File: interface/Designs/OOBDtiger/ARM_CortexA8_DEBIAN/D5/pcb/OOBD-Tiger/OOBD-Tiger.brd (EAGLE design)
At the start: 63.4 x 38.2 mm, 88 parts, among them IC3 DS1307, IC4 DS3231, Q2 32.768kHz, U1 SY6280, U10 MP1482DS, U2 SN65HVD230(SO8), U6 SN65HVD230(SO8)

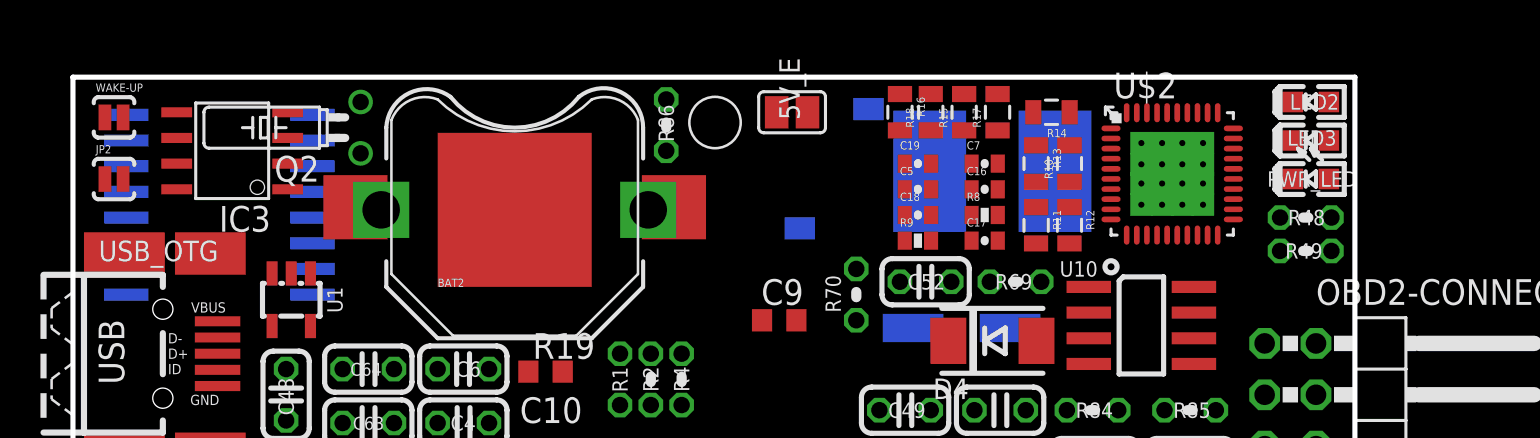
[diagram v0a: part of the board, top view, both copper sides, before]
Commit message: - delete further unneeded files(.lbr) - fix and rename Olimex_Connector.lbr to OOBDtiger-Connector.lbr - fix inconsistency error between schematic and pcb - create regular Projects for AM3352-SOM-EVB and OOBD-Tiger.brd - fix all ERC errors (only some uncritical warnings are open) - update OOBD-Tiger.pdf to visualize current status - fix TLV320AIC3107.lbr (=> but sym and dev is missing)
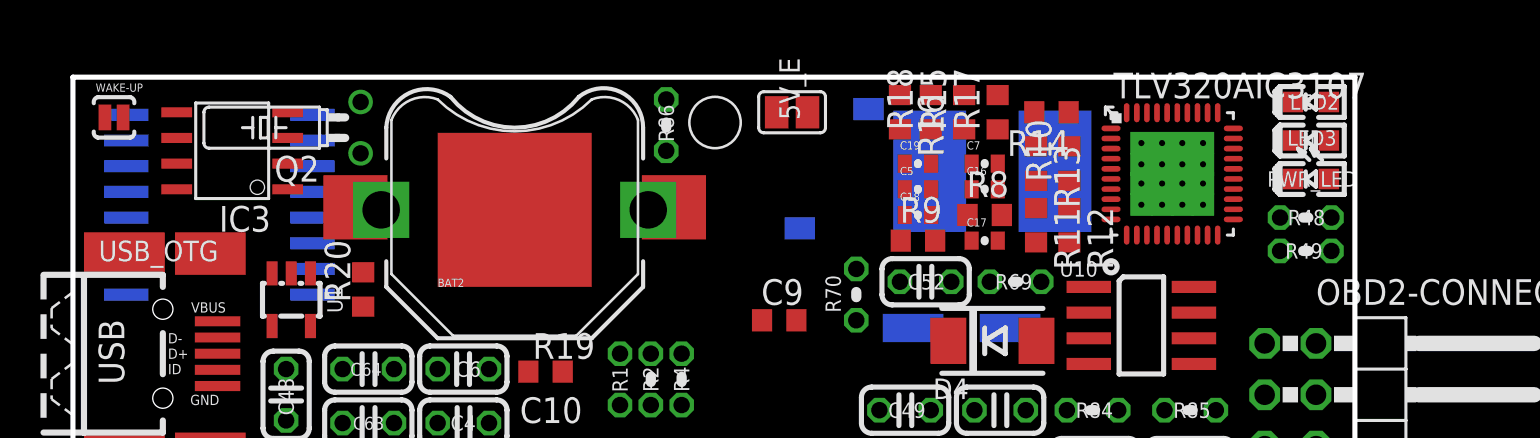
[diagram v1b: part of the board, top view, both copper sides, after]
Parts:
- removed JP2: (no value), SparkFun:SJ_2S-NO
- added R20: 10k, rcl:R0603
- AM3352-SOM-EVB-PLATFORM: device Tiger-connector_new:AM3352-SOM-EVB -> OOBDtiger-Connector:OOBD-TIGER-AM3352-SOM
- R10, R11, R12, R13, R14, R15, R16, R17, R18: device SparkFun-Passives:0805 -> resistor:R0603
- R8, R9: device SparkFun-Passives:0402-RES -> resistor:R0603
- renumbered U$2 to TLV320AIC3107
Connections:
- net P0_12/I2C2_SDA renamed DCAN0_TX
- net P0_13/I2C2_SCL renamed DCAN0_RX
- net P1_8/UART4_RXD renamed DCAN1_TX
- net P1_9/UART4_TXD renamed DCAN1_RX
- net USB1-VBUS renamed USB1_VBUS
- net USB1-VBUS1 renamed USB1_VBUS1
- removed net 3.3V: C16.1, C17.1, R8.2, R9.2, TLV320AIC3107.13, TLV320AIC3107.18, TLV320AIC3107.40
- removed net AIN4: AM3352-SOM-EVB-PLATFORM.4-35
- removed net AIN5: AM3352-SOM-EVB-PLATFORM.4-37
- removed net AIN6: AM3352-SOM-EVB-PLATFORM.4-38
- removed net AIN7: AM3352-SOM-EVB-PLATFORM.4-36
- removed net GNDA: AM3352-SOM-EVB-PLATFORM.4-40
- removed net JTAG_TCK: AM3352-SOM-EVB-PLATFORM.4-29
- removed net JTAG_TDI: AM3352-SOM-EVB-PLATFORM.4-31
- removed net JTAG_TDO: AM3352-SOM-EVB-PLATFORM.4-33
- removed net JTAG_TMS: AM3352-SOM-EVB-PLATFORM.4-32
- removed net JTAG_TRST: AM3352-SOM-EVB-PLATFORM.4-30
- removed net MMC0-SDCD#/EMU4: AM3352-SOM-EVB-PLATFORM.3-17
- removed net N$13: MS-CAN.2
- removed net N$30: L6.2
- removed net NNMI: AM3352-SOM-EVB-PLATFORM.3-22
- removed net OUT: JP2.2
- removed net P0_0/EMDIO: AM3352-SOM-EVB-PLATFORM.3-38
- removed net P0_1/EMDC: AM3352-SOM-EVB-PLATFORM.3-36
- removed net P0_14/UART1_RXD: AM3352-SOM-EVB-PLATFORM.4-6
- removed net P0_15/UART1_TXD: AM3352-SOM-EVB-PLATFORM.4-5
- removed net P0_16/ETXD3: AM3352-SOM-EVB-PLATFORM.3-29
- removed net P0_17/ETXD2: AM3352-SOM-EVB-PLATFORM.3-27
- removed net P0_2/SPI0_SCLK: AM3352-SOM-EVB-PLATFORM.4-11
- removed net P0_20/EMU3: AM3352-SOM-EVB-PLATFORM.4-22
- removed net P0_21/ETXD1: AM3352-SOM-EVB-PLATFORM.3-25
- removed net P0_28/ETXD0: AM3352-SOM-EVB-PLATFORM.3-23
- removed net P0_29/EPHY-RST#/RFCLK: AM3352-SOM-EVB-PLATFORM.3-40
- removed net P0_3/SPI0_D0(MISO): AM3352-SOM-EVB-PLATFORM.4-9
- removed net P0_4/SPI0_D1(MOSI): AM3352-SOM-EVB-PLATFORM.4-10
- removed net P0_5/SPI0_CS0: AM3352-SOM-EVB-PLATFORM.4-12
- removed net P0_7/PWM0_OUT: AM3352-SOM-EVB-PLATFORM.4-27
- removed net P2_18/ERXD3: AM3352-SOM-EVB-PLATFORM.3-30
- removed net P2_19/ERXD2: AM3352-SOM-EVB-PLATFORM.3-28
- removed net P2_20/ERXD1: AM3352-SOM-EVB-PLATFORM.3-26
- removed net P2_21/ERXD0: AM3352-SOM-EVB-PLATFORM.3-24
- removed net P3_0/ECOL: AM3352-SOM-EVB-PLATFORM.3-37
- removed net P3_1/ECRS: AM3352-SOM-EVB-PLATFORM.3-39
- removed net P3_10/ERXCK: AM3352-SOM-EVB-PLATFORM.3-34
- removed net P3_14/SPI1_CLK: AM3352-SOM-EVB-PLATFORM.4-19
- removed net P3_15/SPI1_D0(MISO): AM3352-SOM-EVB-PLATFORM.4-17
- removed net P3_16/SPI1_D1(MOSI): AM3352-SOM-EVB-PLATFORM.4-18
- removed net P3_17/SPI1_CS0: AM3352-SOM-EVB-PLATFORM.4-20
- removed net P3_18/LED1: AM3352-SOM-EVB-PLATFORM.4-21
- removed net P3_2/ERXERR: AM3352-SOM-EVB-PLATFORM.3-35
- removed net P3_3/ETXEN: AM3352-SOM-EVB-PLATFORM.3-31
- removed net P3_4/ERXDV: AM3352-SOM-EVB-PLATFORM.3-32
- removed net P3_5/I2C0-SDA: AM3352-SOM-EVB-PLATFORM.4-16
- removed net P3_6/I2C0-SCL: AM3352-SOM-EVB-PLATFORM.4-15
- removed net P3_7/EMU0: AM3352-SOM-EVB-PLATFORM.4-25
- removed net P3_8/EMU1: AM3352-SOM-EVB-PLATFORM.4-26, R40.2, R7.2
- removed net P3_9/ETXCK: AM3352-SOM-EVB-PLATFORM.3-33
- removed net SCL: IC3.6, IC4.16, R8.1, TLV320AIC3107.1
- removed net SDA: IC3.5, IC4.15
- removed net V+: C9.2, IC4.2, R19.2
- removed net VDDA_ADC: AM3352-SOM-EVB-PLATFORM.4-39
- removed net VREFP: AM3352-SOM-EVB-PLATFORM.4-34
- new net +3V3: C16.1, C17.1, C9.2, IC4.2, R20.2, R8.2, R9.2, TLV320AIC3107.13, TLV320AIC3107.18, TLV320AIC3107.40
- new net HS-CAN_RS: AM3352-SOM-EVB-PLATFORM.4-26, R7.2
- new net I2C0-SCL: AM3352-SOM-EVB-PLATFORM.4-15, IC3.6, IC4.16, R8.1, TLV320AIC3107.1
- new net I2C0-SDA: AM3352-SOM-EVB-PLATFORM.4-16, IC3.5, IC4.15, R9.1, TLV320AIC3107.2
- new net MS-CAN_RS: AM3352-SOM-EVB-PLATFORM.4-25, R40.2
- net +5V: now also R19.2
- net AUD_BCLK: now also AM3352-SOM-EVB-PLATFORM.4-19
- net AUD_DIN: now also AM3352-SOM-EVB-PLATFORM.4-18
- net AUD_DOUT: now also AM3352-SOM-EVB-PLATFORM.4-20
- net AUD_MCLK: now also AM3352-SOM-EVB-PLATFORM.4-24
- net AUD_WCLK: now also AM3352-SOM-EVB-PLATFORM.4-17
- net GND: now also AM3352-SOM-EVB-PLATFORM.4-40
- net N$10: now also MS-CAN.2, R42.1; no longer R9.1, TLV320AIC3107.2
- net N$27: now also IC4.3, R20.1; no longer IC4.4
- net N$29: now also L6.2
- net N$3: no longer IC4.3, JP2.1
- net P3_20/LED2: no longer AM3352-SOM-EVB-PLATFORM.4-23
- net P3_21/LED3: no longer AM3352-SOM-EVB-PLATFORM.4-24
- net SYS_RESETN: now also IC4.4, TLV320AIC3107.31; no longer AM3352-SOM-EVB-PLATFORM.3-21

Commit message: Aufgeräumt mit Mike
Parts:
- removed BAT1: (no value), SparkFun:BATTCON_12MM
- removed IC3: DS1307, PierpaoloSmartSpaceSolutions:SO8
- removed Q2: 32.768kHz, crystal:TC26H
- removed R19: 10k, rcl:R0603
- removed U$3: XTAL32K, PierpaoloSmartSpaceSolutions:FC-135
- C1, C47: device rcl:C025-024X044 -> rcl:C0603_OLIMEX
- R7: device rcl:0204V@1 -> rcl:R0603
- USB_HOST2: device OLIMEX_CONNECTORS:USB_A_VERTICAL_PTH -> OLIMEX_CONNECTORS:USB_PN87520_DEV_PTH
- moved WAKE-UP 8.90 mm to (10.9, 36.7), turned to 180 degrees
- moved USB_OTG 6.37 mm to (3.94, 30.9)
- moved USB_HOST2 2.87 mm to (2.16, 16.1)
- moved HS-CAN 2.29 mm to (1.65, 2.79)
- moved MS-CAN 2.17 mm to (1.78, 6.73)
- moved C1 2.04 mm to (9.14, 8.76)
- moved IC4 1.37 mm to (6.73, 30.6)
- moved C47 0.13 mm to (5.46, 8.76)
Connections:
- removed net N$3: IC3.7, R19.1
- removed net OSCI: IC3.1, Q2.2, U$3.1
- removed net OSCO: IC3.2, Q2.1, U$3.2
- net +5V: no longer IC3.8, R19.2
- net GND: no longer BAT1.GND, IC3.4
- net I2C0-SCL: no longer IC3.6
- net I2C0-SDA: no longer IC3.5
- net N$29: now also USB_HOST2.P$1, USB_HOST2.P$2; no longer USB_HOST2.P$3, USB_HOST2.P$4
- net VBAT: no longer BAT1.PWR@1, IC3.3

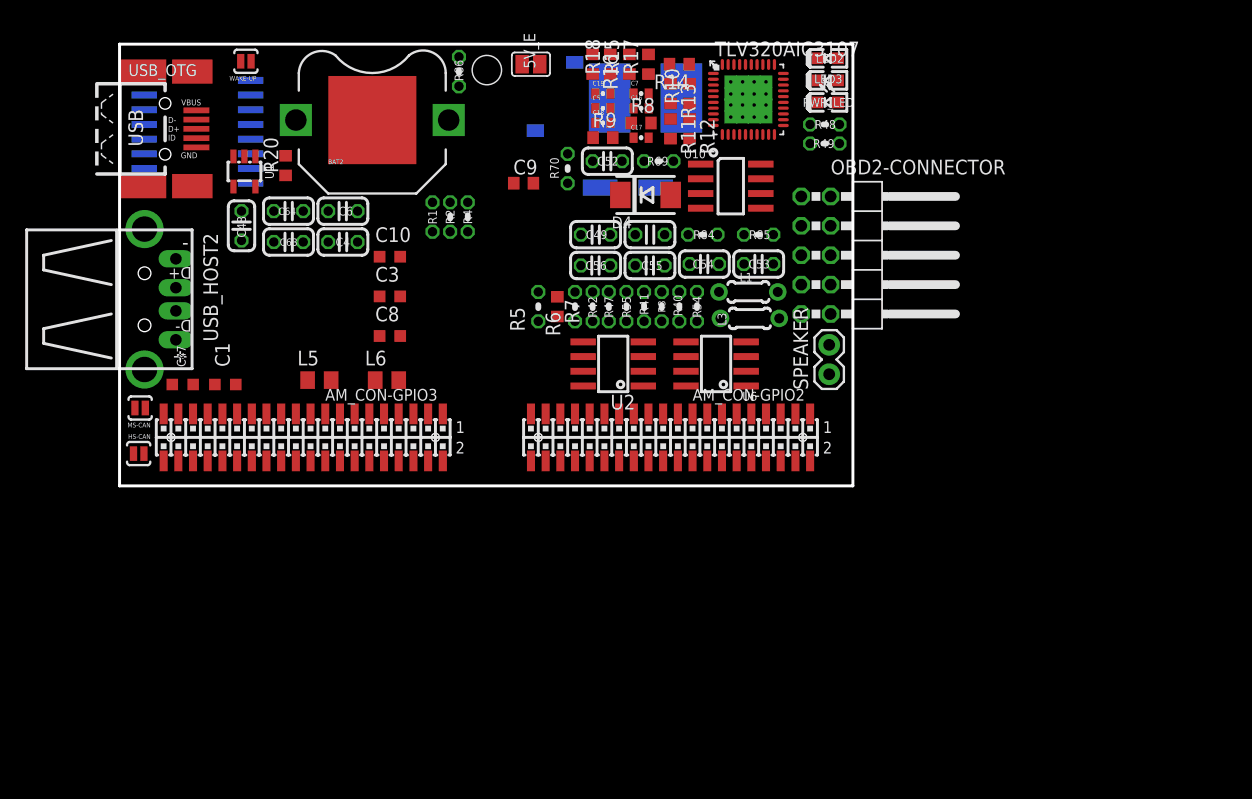
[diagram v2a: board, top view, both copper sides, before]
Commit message: Erster Schritt vereinheitlichen der Packabes, finetuning bzgl. Positionen, Validierung einzelner Signalnamen fortgeschritten aber noch nicht abgeschlossen. Versuchsweise geroutet um ein Gefühl dafür zu bekommen wo Bottlenecks sind
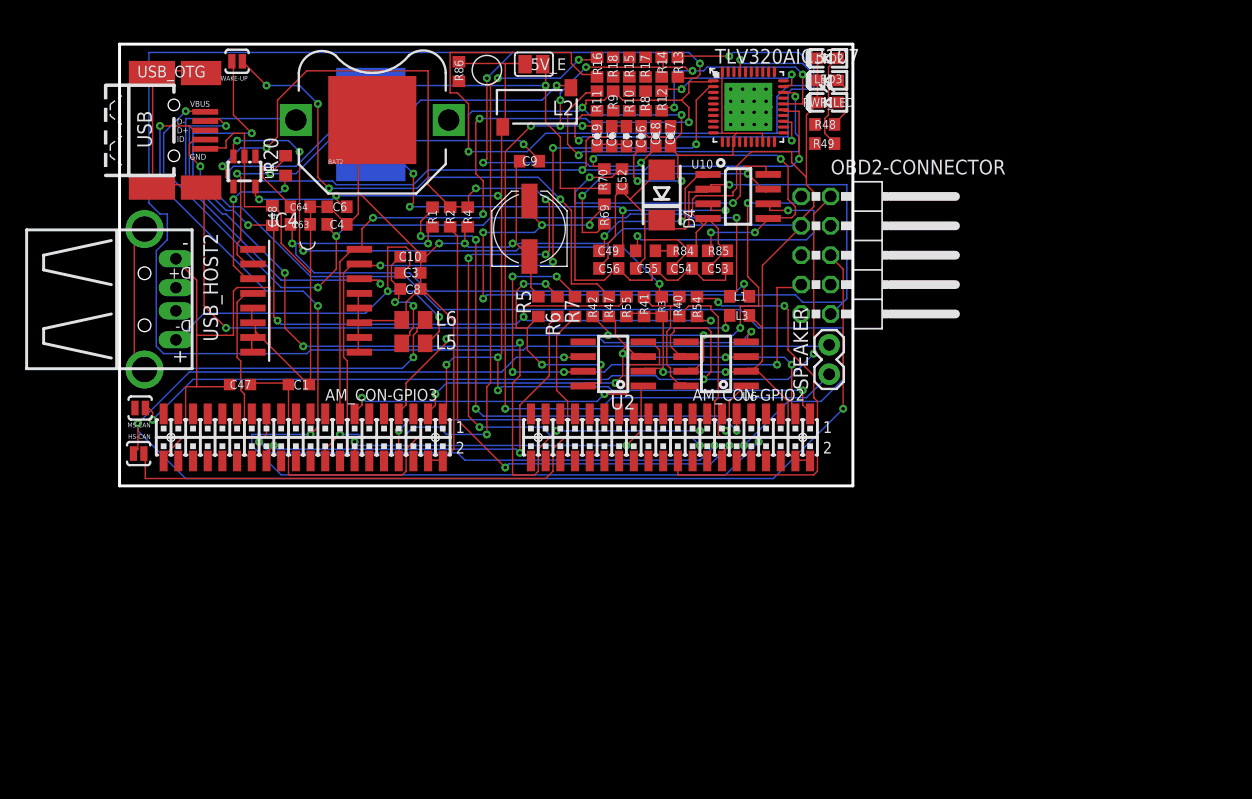
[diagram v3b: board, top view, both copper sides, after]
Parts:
- C16, C17, C18, C19, C5, C7: device SparkFun-Passives:0402-CAP -> SparkFun-Passives:0603-CAP
- C4, C48, C49, C50, C52, C53, C54, C55, C56, C6, C63, C64: device rcl:C025-024X044 -> rcl:C0603
- L1, L3: device rcl:0204/5 -> rcl:L0603
- R1, R2, R3, R4, R40, R41, R42, R47, R48, R49, R5, R54, R55, R6, R69, R70, R84, R85, R86: device rcl:0204V@1 -> rcl:R0603
- moved L11 23.9 mm to (21.7, 31.2), turned to 90 degrees
- moved IC4 17.4 mm to (16.1, 16.0), flipped to the top
- moved C51 9.22 mm to (35.4, 22.2), flipped to the top, turned to 90 degrees
- moved L5 8.73 mm to (25.4, 12.3)
- moved R11 6.79 mm to (41.3, 33.3)
- moved R69 6.56 mm to (41.9, 23.5), turned to 270 degrees
- moved C1 6.35 mm to (15.5, 8.76)
- moved L6 5.69 mm to (25.4, 14.4)
- moved R10 5.25 mm to (44.1, 33.3)
- moved C47 4.95 mm to (10.4, 8.76)
- moved C18 4.71 mm to (46.4, 30.2), turned to 90 degrees
- moved C8 4.44 mm to (25.1, 17.0)
- moved C7 3.90 mm to (43.8, 30.2), turned to 90 degrees
- moved R85 3.82 mm to (51.7, 20.3)
- moved C19 3.72 mm to (41.3, 30.2), turned to 90 degrees
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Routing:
- net GND: track 0.00 -> 302.2 mm, vias 0 -> 5
- net N$15: track 0.00 -> 163.2 mm, vias 0 -> 4
- net CANL1: track 0.00 -> 123.1 mm, vias 0 -> 3
- net +3V3: track 0.00 -> 98.0 mm, vias 0 -> 7
- net N$17: track 0.00 -> 96.6 mm, vias 0 -> 3
- net USB0_DP: track 0.00 -> 96.4 mm, vias 0 -> 4
- net +5V: track 0.00 -> 96.2 mm, vias 0 -> 7
- net USB0-DRV: track 0.00 -> 95.8 mm, vias 0 -> 8
- net CANL: track 0.00 -> 86.6 mm, vias 0 -> 3
- net +12V: track 0.00 -> 83.5 mm, vias 0 -> 5
- net USB0-ID: track 0.00 -> 82.7 mm, vias 0 -> 2
- net N$44: track 0.00 -> 82.5 mm, vias 0 -> 5
- net USB0_DM: track 0.00 -> 79.8 mm, vias 0 -> 6
- net N$266: track 0.00 -> 76.4 mm, vias 0 -> 2
- net VCC: track 0.00 -> 75.0 mm, vias 0 -> 5
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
